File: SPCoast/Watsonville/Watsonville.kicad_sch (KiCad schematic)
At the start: 126 parts, among them SW11 11, SW13 13, SW15 15, SW17 17, SW19 19, SW21 21, SW23 23, SW25 25, SW3 3, SW5 5, SW7 7, SW837 837, SW9 9

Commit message: chore(kicad): masts and maintainer calls carry no CP; IRJ-Signals do; CMRInet Kind is CMRI
Owner decision: an IRJ-Signal is the single source of a signal's control point
(a mast attaches to exactly one IRJ-Signal through its SIGNAL pin); a
maintainer call is tied to its house by the netlist.
- CP dropped from 23 masts and 5 maintainer calls.
- 7 empty IRJ-Signal CPs filled with the plant's only house (Corporal, Sargent).
- 43 empty Name fields that KiCad re-added to Christopher dropped again.
- Codeline-Transport Kind CMRInet -> CMRI on the placed instance and the
  embedded library copy (South-cTc root sheet).

Verified: per-symbol before/after comparison shows only these changes; every
IRJ-Signal in all seven plants has a CP naming one of its plant's houses; net
counts unchanged (Christopher 33, Corporal 26, GilroyCalTrain 27,
GilroyInterchange 22, Luchessa 34, Sargent 18, Watsonville 96, South-cTc 341);
desk compiles to 75 appliances, 137 bindings, 14 columns. Remaining CP
diagnostic: Sargent's Corporal:2NAT placeholder (cross-plant reference).

Co-Authored-By: Claude Sonnet 5.5 <noreply@anthropic.com>
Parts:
- S1, S10, S2, S3, S4, S5, S6, S7, S8, S9: CP Watsonville -> (none)
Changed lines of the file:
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@@
 			)
 		)
-		(property "CP" "Watsonville"
-			(at 40.64 69.85 0)
-			(hide yes)
-			(show_name no)
-			(do_not_autoplace no)
-			(effects
-				(font
-					(size 1.27 1.27)
-				)
-			)
-		)
 		(pin "3"
 		)
@@
 			)
 		)
-		(property "CP" "Watsonville"
-			(at 46.99 82.55 0)
-			(hide yes)
-			(show_name no)
-			(do_not_autoplace no)
-			(effects
-				(font
-					(size 1.27 1.27)
-				)
-			)
-		)
 		(pin "3"
 		)
@@
 			)
 		)
-		(property "CP" "Watsonville"
-			(at 132.08 120.65 0)
-			(hide yes)
-			(show_name no)
-			(do_not_autoplace no)
-			(effects
-				(font
-					(size 1.27 1.27)
-				)
-			)
-		)
 		(pin "1"
 		)
@@
 			)
 		)
-		(property "CP" "Watsonville"
-			(at 85.09 69.85 0)
-			(hide yes)
-			(show_name no)
-			(do_not_autoplace no)
-			(effects
-				(font
-					(size 1.27 1.27)
-				)
-			)
-		)
 		(pin "1"
 		)
@@
 			)
 		)
-		(property "CP" "Watsonville"
-			(at 118.11 105.41 0)
-			(hide yes)
-			(show_name no)
-			(do_not_autoplace no)
-			(effects
-				(font
-					(size 1.27 1.27)
-				)
-			)
-		)
 		(pin "1"
 		)
@@
 			)
 		)
-		(property "CP" "Watsonville"
-			(at 95.25 82.55 0)
-			(hide yes)
-			(show_name no)
-			(do_not_autoplace no)
-			(effects
-				(font
-					(size 1.27 1.27)
-				)
-			)
-		)
 		(pin "1"
 		)
@@
 			)
 		)
-		(property "CP" "Watsonville"
-			(at 102.87 90.17 0)
-			(hide yes)
-			(show_name no)
-			(do_not_autoplace no)
-			(effects
-				(font
-					(size 1.27 1.27)
-				)
-			)
-		)
 		(pin "1"
 		)
@@
 			)
 		)
-		(property "CP" "Watsonville"
-			(at 110.49 97.79 0)
-			(hide yes)
-			(show_name no)
-			(do_not_autoplace no)
-			(effects
-				(font
-					(size 1.27 1.27)
-				)
-			)
-		)
 		(pin "1"
 		)
@@
 			)
 		)
-		(property "CP" "Watsonville"
-			(at 245.11 140.97 0)
-			(hide yes)
-			(show_name no)
-			(do_not_autoplace no)
-			(effects
-				(font
-					(size 1.27 1.27)
-				)
-			)
-		)
 		(pin "1"
 		)
@@
 			(at 125.73 113.03 0)
 			(hide yes)
-			(show_name no)
-			(do_not_autoplace no)
-			(effects
-				(font
-					(size 1.27 1.27)
-				)
-			)
-		)
-		(property "CP" "Watsonville"
-			(at 125.73 113.03 0)
-			(hide yes)

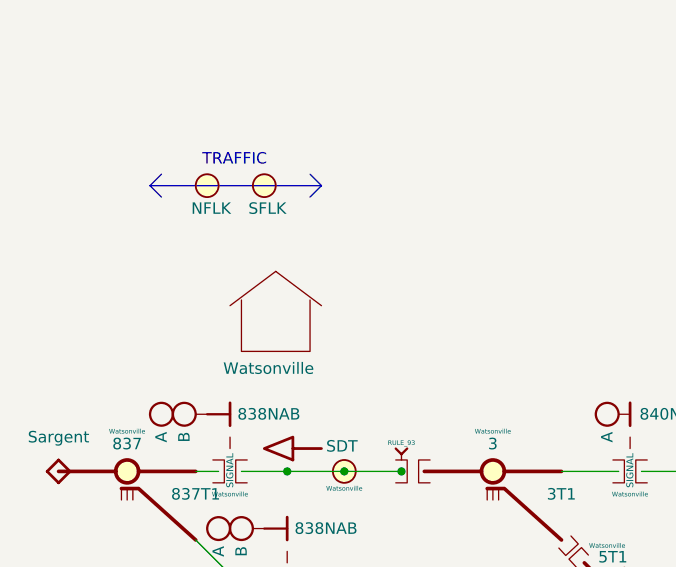
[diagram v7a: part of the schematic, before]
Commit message: SPCoast: owner's edits: Interlocking symbol on every Trackplan; MAIN HOUSE is STRUCTURE/CONTROL_POINT (baseline)
Each plant has one Interlocking symbol (Value is the authoritative name) and
every MAIN HOUSE's Interlocking pin is wired to it. Library Role/Kind:
Interlocking is STRUCTURE/INTERLOCKING, MAIN HOUSE is STRUCTURE/CONTROL_POINT
(refreshed on all instances by the owner).

Verified: one Interlocking symbol per plant; every house shares a net with it;
net counts are one higher than before in each plant (Christopher 34, Corporal
27, GilroyCalTrain 28, GilroyInterchange 23, Luchessa 35, Sargent 19,
Watsonville 97); no root-UUID regression; no symbol moved or removed.

Co-Authored-By: Claude Sonnet 5.5 <noreply@anthropic.com>
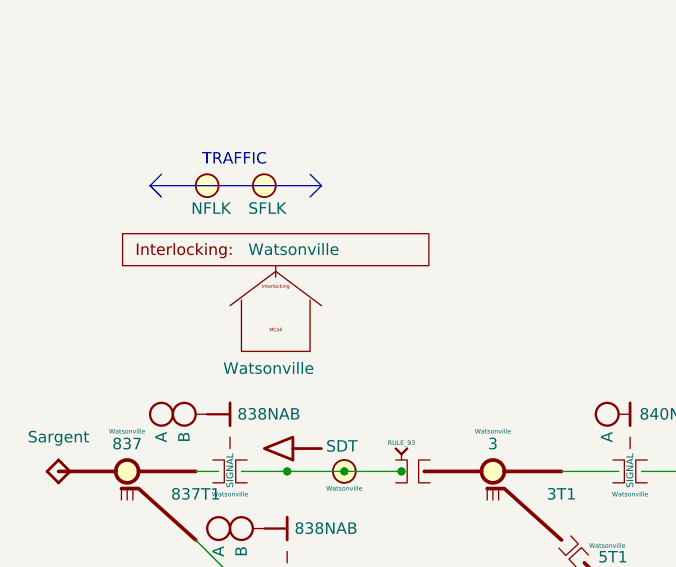
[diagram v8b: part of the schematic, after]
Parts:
- added Plant1: ${TITLE}, symbol Railroad:Interlocking
- HOUSE1: Kind (none) -> CONTROL_POINT; Role CONTROL_POINT -> STRUCTURE
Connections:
- new net: HOUSE1.2 (Interlocking), Plant1.1 (Interlocking)
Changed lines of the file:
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@@
 	)
 	(symbol
+		(lib_id "Railroad:Interlocking")
+		(at 45.72 52.07 0)
+		(unit 1)
+		(body_style 1)
+		(exclude_from_sim no)
+		(in_bom yes)
+		(on_board yes)
+		(in_pos_files yes)
+		(dnp no)
+		(fields_autoplaced yes)
+		(property "Reference" "Plant1"
+			(at 31.496 46.228 0)
+			(hide yes)
+			(show_name no)
+			(do_not_autoplace no)
+			(effects
+				(font
+					(size 1.27 1.27)
+				)
+			)
+		)
+		(property "Value" "${TITLE}"
+			(at 42.672 49.022 0)
+			(show_name no)
+			(do_not_autoplace yes)
+			(effects
+				(font
+					(size 1.27 1.27)
+				)
+				(justify left)
+			)
+		)
+		(property "Footprint" ""
+			(at 45.72 52.07 0)
+			(hide yes)
+			(show_name no)
+			(do_not_autoplace no)
+			(effects
+				(font
+					(size 1.27 1.27)
+				)
+			)
+		)
+		(property "Datasheet" ""
+			(at 45.72 52.07 0)
+			(hide yes)
+			(show_name no)
+			(do_not_autoplace no)
+			(effects
+				(font
+					(size 1.27 1.27)
+				)
+			)
+		)
+		(property "Description" ""
+			(at 45.72 52.07 0)
+			(hide yes)
+			(show_name no)
+			(do_not_autoplace no)
+			(effects
+				(font
+					(size 1.27 1.27)
+				)
+			)
+		)
+		(property "Role" "STRUCTURE"
+			(at 34.417 42.418 0)
+			(hide yes)
+			(show_name no)
+			(do_not_autoplace no)
+			(effects
+				(font
+					(size 1.27 1.27)
+				)
+			)
+		)
+		(property "Kind" "INTERLOCKING"
+			(at 35.814 44.069 0)
+			(hide yes)
+			(show_name no)
+			(do_not_autoplace no)
+			(effects
+				(font
+					(size 1.27 1.27)
+				)
+			)
+		)
+		(pin "1"
+		)
+		(instances
+			(project "Watsonville"
+				(path "/773cfd5d-7233-47b3-8f6c-03be10f2d31c"
+					(reference "Plant1")
+					(unit 1)
+				)
+			)
+		)
+	)
+	(symbol
 		(lib_id "Railroad:Switch_Powered_Diag")
 		(at 82.55 86.36 0)
@@
 			)
 		)
-		(property "Description" "Rrepresents the Control Point Maintainer Bungalow (plus optional Maintainer Call)"
+		(property "Description" "The Control Point Maintainer Bungalow (plus optional Maintainer Call)"
 			(at 45.72 62.865 0)
 			(hide yes)
@@
 		)
 		(property "Milepost" "83.7"
-			(at 45.72 62.87 0)
+			(at 45.72 62.865 0)
 			(hide yes)
 			(show_name no)
@@
 			)
 		)
-		(property "Role" "CONTROL_POINT"
-			(at 45.72 57.15 0)
+		(property "Role" "STRUCTURE"
+			(at 30.48 54.61 0)
+			(hide yes)
+			(show_name no)
+			(do_not_autoplace no)
+			(effects
+				(font
+					(size 1.27 1.27)
+				)
+			)
+		)
+		(property "Kind" "CONTROL_POINT"
+			(at 32.385 56.642 0)
 			(hide yes)
 			(show_name no)
@@
 		(pin "1"
 		)
+		(pin "2"
+		)
 		(instances
